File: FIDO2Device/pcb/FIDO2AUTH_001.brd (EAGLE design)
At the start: 30 x 30 mm, 1 part, among them U1 MDBT50Q-P1M

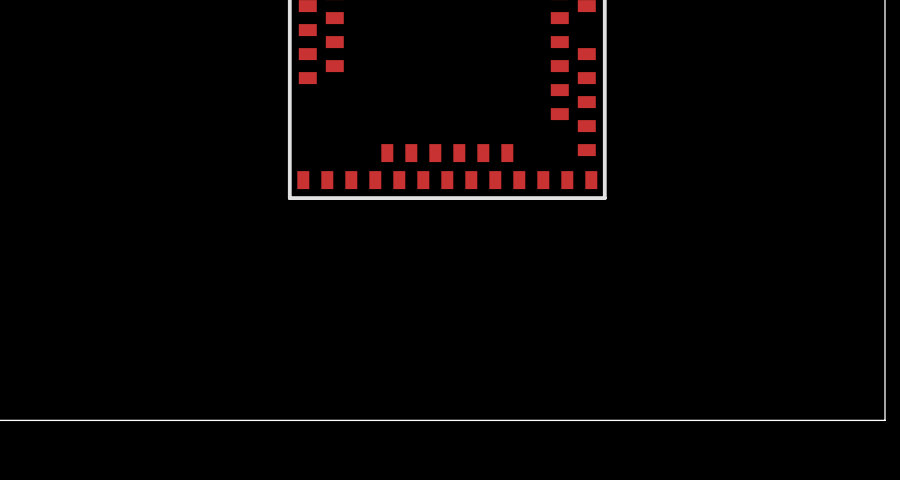
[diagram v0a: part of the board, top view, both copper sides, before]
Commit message: [WIP] ブレークアウト基板回路図
・クリスタル、バイパスコンデンサーを追加配置
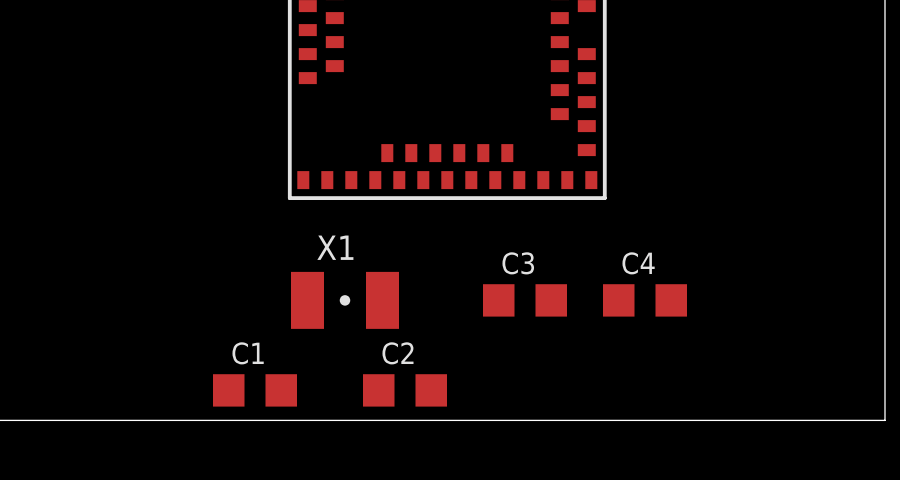
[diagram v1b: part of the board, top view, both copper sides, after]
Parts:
- added C1, C2: 12pF, Parts:C0603K
- added C3, C4: 4.7uF, Parts:C0603K
- added X1: NX3215SA-32.768K, Parts:NX3215
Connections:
- new net 0V: C1.2, C2.2, C3.2, C4.2, U1.1, U1.15, U1.2, U1.33, U1.55
- new net DCCH: U1.31
- new net D_N: U1.34
- new net D_P: U1.35
- new net NFC1: U1.52
- new net NFC2: U1.54
- new net RESET: U1.40
- new net SWDCLK: U1.53
- new net SWDIO: U1.51
- new net VBUS: C4.1, U1.32
- new net VDD: C3.1, U1.28
- new net VDDH: U1.30
- new net XL1: C1.1, U1.17, X1.1
- new net XL2: C2.1, U1.18, X1.2
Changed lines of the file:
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@@
 <setting verticaltext="up"/>
 </settings>
-<grid distance="1" unitdist="mm" unit="mm" style="lines" multiple="1" display="yes" altdistance="0.025" altunitdist="inch" altunit="inch"/>
+<grid distance="25" unitdist="mil" unit="mil" style="lines" multiple="1" display="yes" altdistance="0.025" altunitdist="inch" altunit="inch"/>
 <layers>
 <layer number="1" name="Top" color="4" fill="1" visible="yes" active="yes"/>
@@
 <layer number="27" name="tValues" color="7" fill="1" visible="no" active="yes"/>
 <layer number="28" name="bValues" color="7" fill="1" visible="no" active="yes"/>
-<layer number="29" name="tStop" color="7" fill="3" visible="no" active="yes"/>
-<layer number="30" name="bStop" color="7" fill="6" visible="no" active="yes"/>
-<layer number="31" name="tCream" color="7" fill="4" visible="no" active="yes"/>
-<layer number="32" name="bCream" color="7" fill="5" visible="no" active="yes"/>
+<layer number="29" name="tStop" color="7" fill="3" visible="yes" active="yes"/>
+<layer number="30" name="bStop" color="7" fill="6" visible="yes" active="yes"/>
+<layer number="31" name="tCream" color="7" fill="4" visible="yes" active="yes"/>
+<layer number="32" name="bCream" color="7" fill="5" visible="yes" active="yes"/>
 <layer number="33" name="tFinish" color="6" fill="3" visible="no" active="yes"/>
 <layer number="34" name="bFinish" color="6" fill="6" visible="no" active="yes"/>
@@
 <elements>
 <element name="U1" library="Parts" package="MDBT50Q-P1M" value="MDBT50Q-P1M" x="15.41" y="15.16"/>
+<element name="X1" library="Parts" package="NX3215" value="NX3215SA-32.768K" x="12" y="4"/>
+<element name="C1" library="Parts" package="C0603K" value="12pF" x="9" y="1"/>
+<element name="C2" library="Parts" package="C0603K" value="12pF" x="14" y="1"/>
+<element name="C3" library="Parts" package="C0603K" value="4.7uF" x="18" y="4"/>
+<element name="C4" library="Parts" package="C0603K" value="4.7uF" x="22" y="4"/>
 </elements>
 <signals>
+<signal name="0V">
+<contactref element="C1" pad="2"/>
+<contactref element="C2" pad="2"/>
+<contactref element="C3" pad="2"/>
+<contactref element="C4" pad="2"/>
+<contactref element="U1" pad="15"/>
+<contactref element="U1" pad="33"/>
+<contactref element="U1" pad="55"/>
+<contactref element="U1" pad="1"/>
+<contactref element="U1" pad="2"/>
+<wire x1="10.76" y1="18.91" x2="20.06" y2="18.91" width="0" layer="19" extent="1-1"/>
+<wire x1="10.76" y1="17.81" x2="10.76" y2="18.91" width="0" layer="19" extent="1-1"/>
+<wire x1="10.61" y1="8.01" x2="10.76" y2="17.81" width="0" layer="19" extent="1-1"/>
+<wire x1="20.21" y1="8.01" x2="10.61" y2="8.01" width="0" layer="19" extent="1-1"/>
+<wire x1="9.875" y1="1" x2="10.61" y2="8.01" width="0" layer="19" extent="1-1"/>
+<wire x1="14.875" y1="1" x2="9.875" y2="1" width="0" layer="19" extent="1-1"/>
+<wire x1="18.875" y1="4" x2="14.875" y2="1" width="0" layer="19" extent="1-1"/>
+<wire x1="22.875" y1="4" x2="18.875" y2="4" width="0" layer="19" extent="1-1"/>
+</signal>
+<signal name="XL1">
+<contactref element="X1" pad="1"/>
+<contactref element="C1" pad="1"/>
+<contactref element="U1" pad="17"/>
+<wire x1="10.75" y1="4" x2="12.21" y2="8.01" width="0" layer="19" extent="1-1"/>
+<wire x1="8.125" y1="1" x2="10.75" y2="4" width="0" layer="19" extent="1-1"/>
+</signal>
+<signal name="XL2">
+<contactref element="X1" pad="2"/>
+<contactref element="C2" pad="1"/>
+<contactref element="U1" pad="18"/>
+<wire x1="13.25" y1="4" x2="13.01" y2="8.01" width="0" layer="19" extent="1-1"/>
+<wire x1="13.125" y1="1" x2="13.25" y2="4" width="0" layer="19" extent="1-1"/>
+</signal>
+<signal name="VDD">
+<contactref element="C3" pad="1"/>
+<contactref element="U1" pad="28"/>
+<wire x1="17.125" y1="4" x2="17.01" y2="8.01" width="0" layer="19" extent="1-1"/>
+</signal>
+<signal name="VBUS">
+<contactref element="C4" pad="1"/>
+<contactref element="U1" pad="32"/>
+<wire x1="21.125" y1="4" x2="19.41" y2="8.01" width="0" layer="19" extent="1-1"/>
+</signal>
+<signal name="SWDCLK">
+<contactref element="U1" pad="53"/>
+</signal>
+<signal name="NFC1">
+<contactref element="U1" pad="52"/>
+</signal>
+<signal name="NFC2">
+<contactref element="U1" pad="54"/>
+</signal>
+<signal name="SWDIO">
+<contactref element="U1" pad="51"/>
+</signal>
+<signal name="RESET">
+<contactref element="U1" pad="40"/>
+</signal>
+<signal name="D_P">
+<contactref element="U1" pad="35"/>
+</signal>
+<signal name="D_N">
+<contactref element="U1" pad="34"/>
+</signal>
+<signal name="VDDH">
+<contactref element="U1" pad="30"/>
+</signal>
+<signal name="DCCH">
+<contactref element="U1" pad="31"/>
+</signal>
 </signals>
 </board>

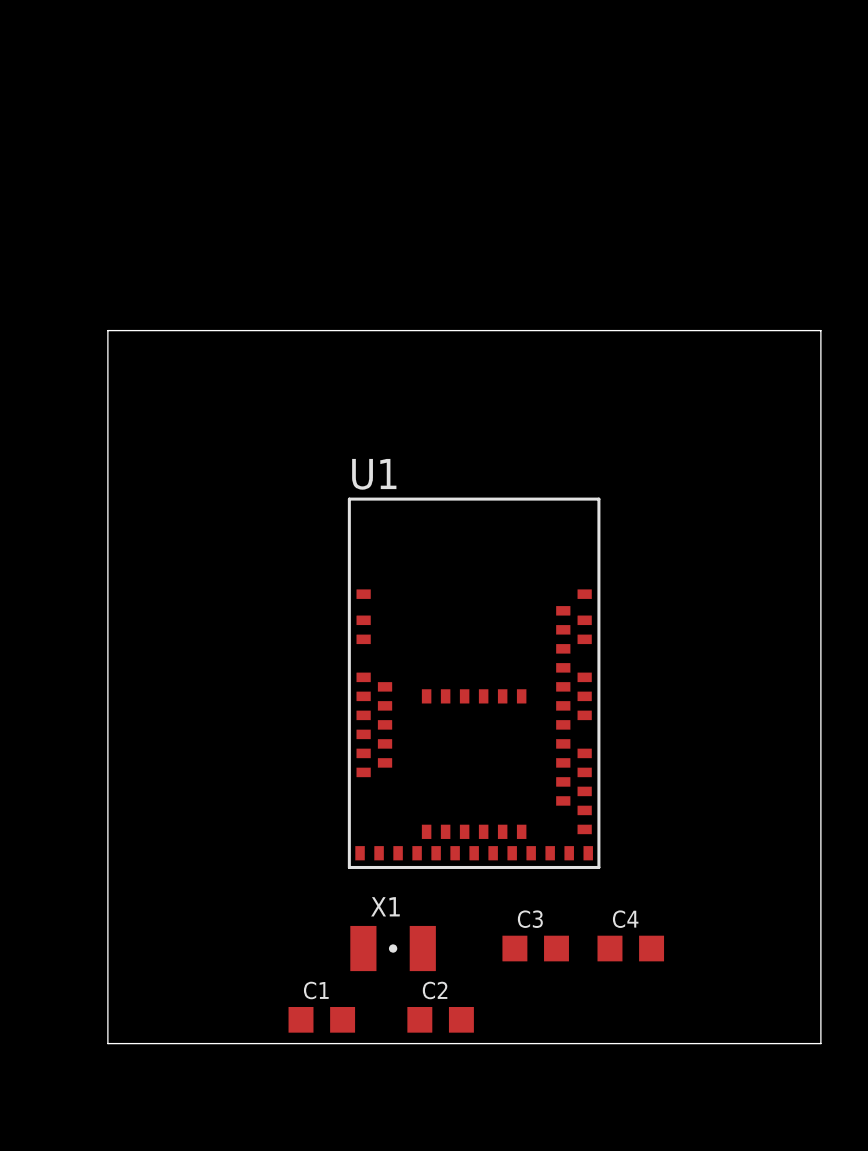
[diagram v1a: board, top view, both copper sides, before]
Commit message: [WIP] ブレークアウト基板回路図
・USBプラグ部を追加
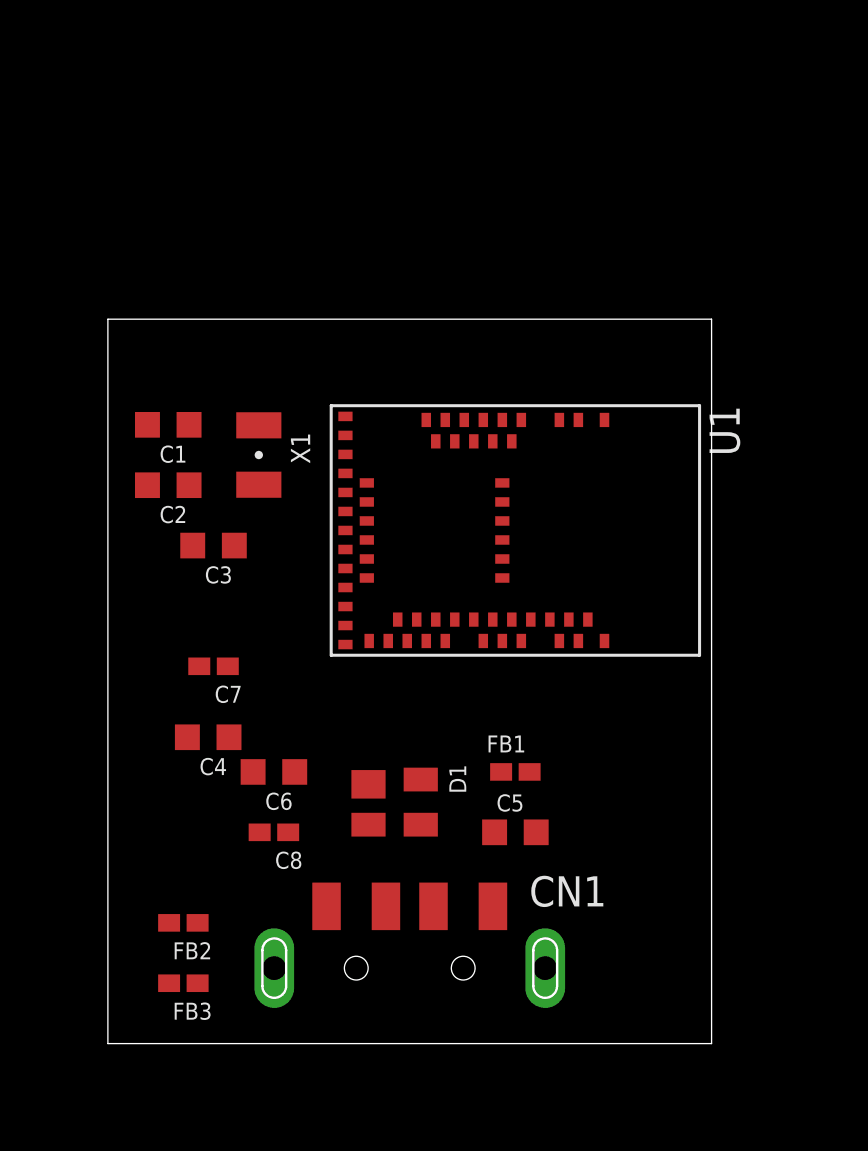
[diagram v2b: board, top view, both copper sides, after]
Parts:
- added C5, C6: 10uF, Parts:C0603K
- added C7, C8: 0.1uF, Parts:C0402K
- added CN1: TE-1734028, Connectors:TE-1734028
- added D1: PRTR5V0U2X, Parts:SOT143B
- added FB1, FB2, FB3: BLM15AG121SN1D, Parts:C0402K
- moved C1 25.9 mm to (2.54, 26.0), turned to 180 degrees
- moved C2 25.2 mm to (2.54, 23.5), turned to 180 degrees
- moved C3 21.7 mm to (4.45, 21.0), turned to 180 degrees
- moved X1 21.5 mm to (6.35, 24.8), turned to 270 degrees
- moved C4 19.9 mm to (4.22, 12.9), turned to 180 degrees
- moved U1 6.66 mm to (17.1, 21.6), turned to 270 degrees
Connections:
- removed net DCCH: U1.31
- removed net VBUS: C4.1, U1.32
- removed net VDD: C3.1, U1.28
- removed net VDDH: U1.30
- new net N$1: C5.1, C6.1, C8.1, CN1.1, D1.4, FB1.1
- new net N$2: CN1.4, FB2.1
- new net N$3: CN1.FG1, CN1.FG2, FB3.1
- new net VBUS_NRF: C4.1, C7.1, FB1.2, U1.32
- new net VDD_NRF: C3.1, U1.28, U1.30
- net 0V: now also C5.2, C6.2, C7.2, C8.2, D1.1, FB2.2, FB3.2
- net D_N: now also CN1.2, D1.2
- net D_P: now also CN1.3, D1.3
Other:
- board size 30 x 30 mm -> 25.4 x 30.5 mm
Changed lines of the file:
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@@
 <board>
 <plain>
-<wire x1="0" y1="0" x2="30" y2="0" width="0" layer="20"/>
-<wire x1="30" y1="0" x2="30" y2="30" width="0" layer="20"/>
-<wire x1="30" y1="30" x2="0" y2="30" width="0" layer="20"/>
-<wire x1="0" y1="30" x2="0" y2="0" width="0" layer="20"/>
+<wire x1="0" y1="0" x2="25.4" y2="0" width="0" layer="20"/>
+<wire x1="25.4" y1="0" x2="25.4" y2="30.48" width="0" layer="20"/>
+<wire x1="25.4" y1="30.48" x2="0" y2="30.48" width="0" layer="20"/>
+<wire x1="0" y1="30.48" x2="0" y2="0" width="0" layer="20"/>
 </plain>
 <attributes>
@@
 </autorouter>
 <elements>
-<element name="U1" library="Parts" package="MDBT50Q-P1M" value="MDBT50Q-P1M" x="15.41" y="15.16"/>
-<element name="X1" library="Parts" package="NX3215" value="NX3215SA-32.768K" x="12" y="4"/>
-<element name="C1" library="Parts" package="C0603K" value="12pF" x="9" y="1"/>
-<element name="C2" library="Parts" package="C0603K" value="12pF" x="14" y="1"/>
-<element name="C3" library="Parts" package="C0603K" value="4.7uF" x="18" y="4"/>
-<element name="C4" library="Parts" package="C0603K" value="4.7uF" x="22" y="4"/>
+<element name="U1" library="Parts" package="MDBT50Q-P1M" value="MDBT50Q-P1M" x="17.145" y="21.59" rot="R270"/>
+<element name="X1" library="Parts" package="NX3215" value="NX3215SA-32.768K" x="6.35" y="24.765" rot="R270"/>
+<element name="C1" library="Parts" package="C0603K" value="12pF" x="2.54" y="26.035" rot="R180"/>
+<element name="C2" library="Parts" package="C0603K" value="12pF" x="2.54" y="23.495" rot="R180"/>
+<element name="C3" library="Parts" package="C0603K" value="4.7uF" x="4.445" y="20.955" rot="R180"/>
+<element name="C4" library="Parts" package="C0603K" value="4.7uF" x="4.22" y="12.89" rot="R180"/>
+<element name="FB1" library="Parts" package="C0402K" value="BLM15AG121SN1D" x="17.145" y="11.43"/>
+<element name="FB2" library="Parts" package="C0402K" value="BLM15AG121SN1D" x="3.175" y="5.08" rot="R180"/>
+<element name="C5" library="Parts" package="C0603K" value="10uF" x="17.145" y="8.89"/>
+<element name="C6" library="Parts" package="C0603K" value="10uF" x="6.985" y="11.43" rot="R180"/>
+<element name="C7" library="Parts" package="C0402K" value="0.1uF" x="4.445" y="15.875" rot="R180"/>
+<element name="C8" library="Parts" package="C0402K" value="0.1uF" x="6.985" y="8.89" rot="R180"/>
+<element name="FB3" library="Parts" package="C0402K" value="BLM15AG121SN1D" x="3.175" y="2.54" rot="R180"/>
+<element name="D1" library="Parts" package="SOT143B" value="PRTR5V0U2X" x="12.065" y="10.16" rot="R270"/>
+<element name="CN1" library="Connectors" package="TE-1734028" value="TE-1734028" x="12.7" y="3.175" smashed="yes">
+<attribute name="NAME" x="17.725" y="5.77" size="1.27" layer="25"/>
+<attribute name="VALUE" x="8.2" y="-1.325" size="1.27" layer="27"/>
+</element>
 </elements>
 <signals>
@@
 <contactref element="U1" pad="1"/>
 <contactref element="U1" pad="2"/>
-<wire x1="10.76" y1="18.91" x2="20.06" y2="18.91" width="0" layer="19" extent="1-1"/>
-<wire x1="10.76" y1="17.81" x2="10.76" y2="18.91" width="0" layer="19" extent="1-1"/>
-<wire x1="10.61" y1="8.01" x2="10.76" y2="17.81" width="0" layer="19" extent="1-1"/>
-<wire x1="20.21" y1="8.01" x2="10.61" y2="8.01" width="0" layer="19" extent="1-1"/>
-<wire x1="9.875" y1="1" x2="10.61" y2="8.01" width="0" layer="19" extent="1-1"/>
-<wire x1="14.875" y1="1" x2="9.875" y2="1" width="0" layer="19" extent="1-1"/>
-<wire x1="18.875" y1="4" x2="14.875" y2="1" width="0" layer="19" extent="1-1"/>
-<wire x1="22.875" y1="4" x2="18.875" y2="4" width="0" layer="19" extent="1-1"/>
+<contactref element="C5" pad="2"/>
+<contactref element="C7" pad="2"/>
+<contactref element="FB2" pad="2"/>
+<contactref element="FB3" pad="2"/>
+<contactref element="D1" pad="1"/>
+<contactref element="C8" pad="2"/>
+<contactref element="C6" pad="2"/>
+<wire x1="19.795" y1="26.24" x2="20.895" y2="26.24" width="0" layer="19" extent="1-1"/>
+<wire x1="20.895" y1="16.94" x2="20.895" y2="26.24" width="0" layer="19" extent="1-1"/>
+<wire x1="18.02" y1="8.89" x2="20.895" y2="16.94" width="0" layer="19" extent="1-1"/>
+<wire x1="10.965" y1="10.91" x2="18.02" y2="8.89" width="0" layer="19" extent="1-1"/>
+<wire x1="6.11" y1="11.43" x2="10.965" y2="10.91" width="0" layer="19" extent="1-1"/>
+<wire x1="6.385" y1="8.89" x2="6.11" y2="11.43" width="0" layer="19" extent="1-1"/>
+<wire x1="3.345" y1="12.89" x2="6.11" y2="11.43" width="0" layer="19" extent="1-1"/>
+<wire x1="3.845" y1="15.875" x2="3.345" y2="12.89" width="0" layer="19" extent="1-1"/>
+<wire x1="3.57" y1="20.955" x2="3.845" y2="15.875" width="0" layer="19" extent="1-1"/>
+<wire x1="1.665" y1="23.495" x2="3.57" y2="20.955" width="0" layer="19" extent="1-1"/>
+<wire x1="1.665" y1="26.035" x2="1.665" y2="23.495" width="0" layer="19" extent="1-1"/>
+<wire x1="2.575" y1="5.08" x2="6.385" y2="8.89" width="0" layer="19" extent="1-1"/>
+<wire x1="2.575" y1="2.54" x2="2.575" y2="5.08" width="0" layer="19" extent="1-1"/>
+<wire x1="9.995" y1="16.79" x2="10.965" y2="10.91" width="0" layer="19" extent="1-1"/>
+<wire x1="9.995" y1="26.39" x2="1.665" y2="26.035" width="0" layer="19" extent="1-1"/>
 </signal>
 <signal name="XL1">
@@
 <contactref element="C1" pad="1"/>
 <contactref element="U1" pad="17"/>
-<wire x1="10.75" y1="4" x2="12.21" y2="8.01" width="0" layer="19" extent="1-1"/>
-<wire x1="8.125" y1="1" x2="10.75" y2="4" width="0" layer="19" extent="1-1"/>
+<wire x1="3.415" y1="26.035" x2="6.35" y2="26.015" width="0" layer="19" extent="1-1"/>
+<wire x1="9.995" y1="24.79" x2="6.35" y2="26.015" width="0" layer="19" extent="1-1"/>
 </signal>
 <signal name="XL2">
@@
 <contactref element="C2" pad="1"/>
 <contactref element="U1" pad="18"/>
-<wire x1="13.25" y1="4" x2="13.01" y2="8.01" width="0" layer="19" extent="1-1"/>
-<wire x1="13.125" y1="1" x2="13.25" y2="4" width="0" layer="19" extent="1-1"/>
-</signal>
-<signal name="VDD">
-<contactref element="C3" pad="1"/>
-<contactref element="U1" pad="28"/>
-<wire x1="17.125" y1="4" x2="17.01" y2="8.01" width="0" layer="19" extent="1-1"/>
-</signal>
-<signal name="VBUS">
+<wire x1="6.35" y1="23.515" x2="9.995" y2="23.99" width="0" layer="19" extent="1-1"/>
+<wire x1="3.415" y1="23.495" x2="6.35" y2="23.515" width="0" layer="19" extent="1-1"/>
+</signal>
+<signal name="VBUS_NRF">
 <contactref element="C4" pad="1"/>
 <contactref element="U1" pad="32"/>
-<wire x1="21.125" y1="4" x2="19.41" y2="8.01" width="0" layer="19" extent="1-1"/>
+<contactref element="FB1" pad="2"/>
+<contactref element="C7" pad="1"/>
+<wire x1="9.995" y1="17.59" x2="17.745" y2="11.43" width="0" layer="19" extent="1-1"/>
+<wire x1="5.045" y1="15.875" x2="9.995" y2="17.59" width="0" layer="19" extent="1-1"/>
+<wire x1="5.095" y1="12.89" x2="5.045" y2="15.875" width="0" layer="19" extent="1-1"/>
 </signal>
 <signal name="SWDCLK">
@@
 <signal name="D_P">
 <contactref element="U1" pad="35"/>
+<contactref element="D1" pad="3"/>
+<contactref element="CN1" pad="3"/>
+<wire x1="13.165" y1="9.21" x2="11.795" y2="16.94" width="0" layer="19" extent="1-1"/>
+<wire x1="11.7" y1="5.775" x2="13.165" y2="9.21" width="0" layer="19" extent="1-1"/>
 </signal>
 <signal name="D_N">
 <contactref element="U1" pad="34"/>
-</signal>
-<signal name="VDDH">
+<contactref element="D1" pad="2"/>
+<contactref element="CN1" pad="2"/>
+<wire x1="10.965" y1="9.21" x2="10.995" y2="16.94" width="0" layer="19" extent="1-1"/>
+<wire x1="13.7" y1="5.775" x2="10.965" y2="9.21" width="0" layer="19" extent="1-1"/>
+</signal>
+<signal name="VDD_NRF">
+<contactref element="U1" pad="28"/>
+<contactref element="C3" pad="1"/>
 <contactref element="U1" pad="30"/>
-</signal>
-<signal name="DCCH">
-<contactref element="U1" pad="31"/>
+<wire x1="9.995" y1="19.19" x2="9.995" y2="19.99" width="0" layer="19" extent="1-1"/>
+<wire x1="5.32" y1="20.955" x2="9.995" y2="19.99" width="0" layer="19" extent="1-1"/>
+</signal>
+<signal name="N$1">
+<contactref element="FB1" pad="1"/>
+<contactref element="C5" pad="1"/>
+<contactref element="C8" pad="1"/>
+<contactref element="C6" pad="1"/>
+<contactref element="CN1" pad="1"/>
+<contactref element="D1" pad="4"/>
+<wire x1="16.27" y1="8.89" x2="16.545" y2="11.43" width="0" layer="19" extent="1-1"/>
+<wire x1="16.2" y1="5.775" x2="16.27" y2="8.89" width="0" layer="19" extent="1-1"/>
+<wire x1="13.165" y1="11.11" x2="16.545" y2="11.43" width="0" layer="19" extent="1-1"/>
+<wire x1="7.86" y1="11.43" x2="13.165" y2="11.11" width="0" layer="19" extent="1-1"/>
+<wire x1="7.585" y1="8.89" x2="7.86" y2="11.43" width="0" layer="19" extent="1-1"/>
+</signal>
+<signal name="N$2">
+<contactref element="FB2" pad="1"/>
+<contactref element="CN1" pad="4"/>
+<wire x1="3.775" y1="5.08" x2="9.2" y2="5.775" width="0" layer="19" extent="1-1"/>
+</signal>
+<signal name="N$3">
+<contactref element="FB3" pad="1"/>
+<contactref element="CN1" pad="FG1"/>
+<contactref element="CN1" pad="FG2"/>
+<wire x1="7" y1="3.175" x2="18.4" y2="3.175" width="0" layer="19" extent="1-1"/>
+<wire x1="3.775" y1="2.54" x2="7" y2="3.175" width="0" layer="19" extent="1-1"/>
 </signal>
 </signals>
